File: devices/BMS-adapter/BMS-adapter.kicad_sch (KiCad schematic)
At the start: 5 parts, among them J1 Conn_01x05, J2 Conn_01x05, J3 Conn_01x02, J4 Conn_01x02, SW1 SW_SPST

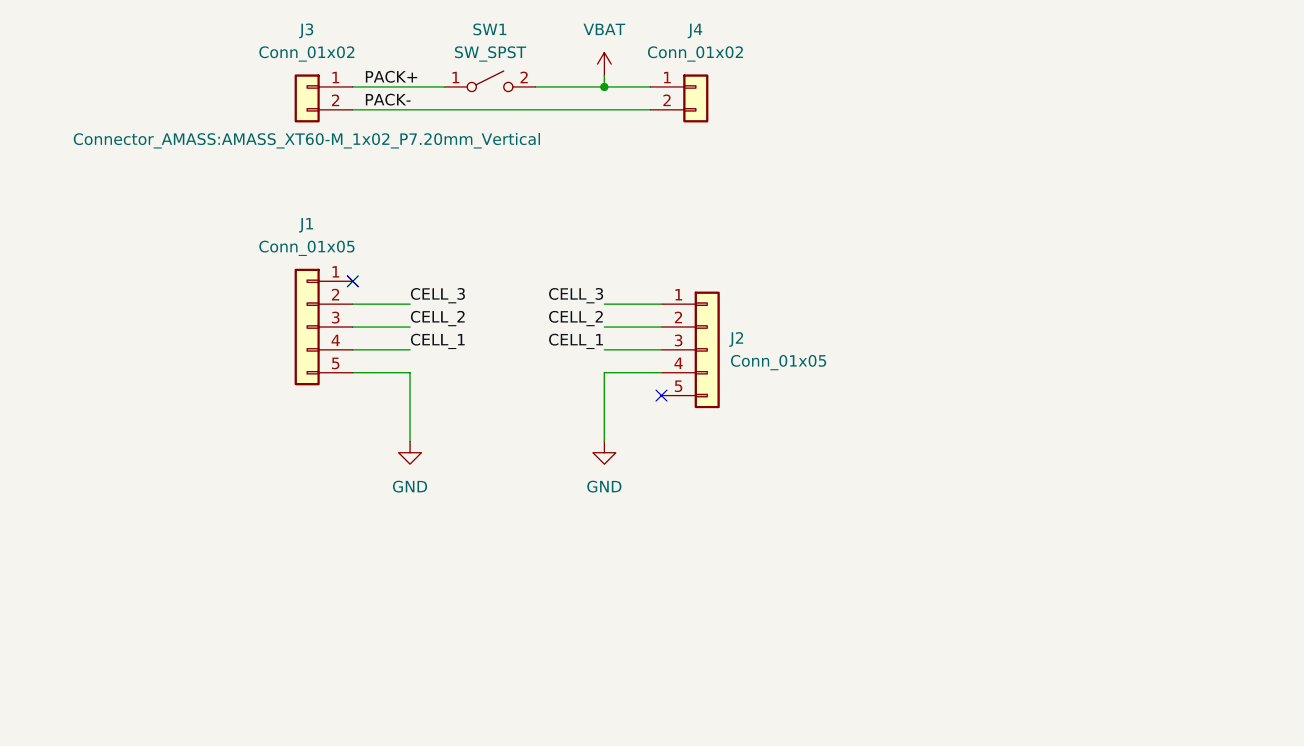
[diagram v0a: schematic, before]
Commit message: Adds a PowerJack
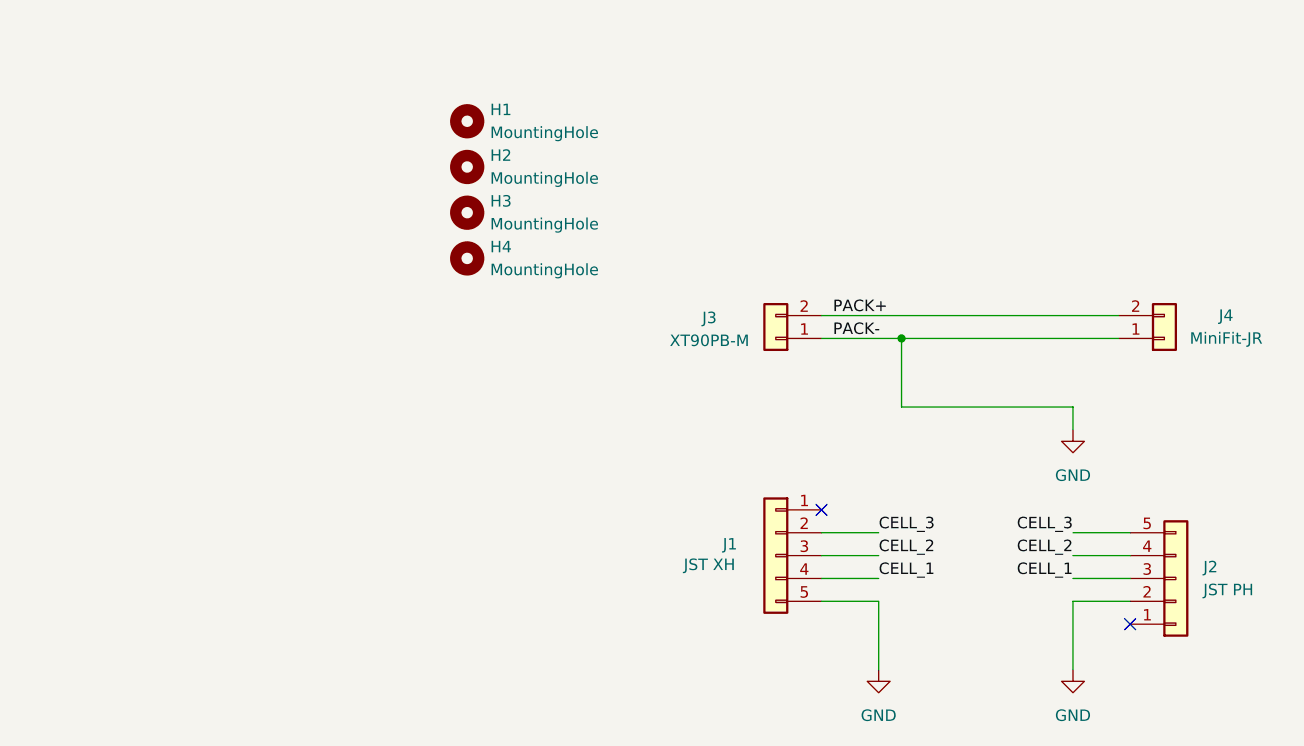
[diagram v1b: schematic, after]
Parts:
- removed SW1: SW_SPST, symbol Switch:SW_SPST
- added H1, H2, H3, H4: MountingHole, MountingHole:MountingHole_3.2mm_M3_DIN965, symbol Mechanical:MountingHole
- J1: value Conn_01x05 -> JST XH; MPN (none) -> B5B-XH-AM
- J2: value Conn_01x05 -> JST PH; MPN (none) -> B5B-PH-K
- J3: value Conn_01x02 -> XT90PB-M; footprint Connector_AMASS:AMASS_XT60-M_1x02_P7.20mm_Vertical -> common:XT90PB-M; MPN (none) -> XT90PB-M
- J4: value Conn_01x02 -> MiniFit-JR; footprint (none) -> Connector_Molex:Molex_Mini-Fit_Jr_5566-02A_2x01_P4.20mm_Vertical; MPN (none) -> 0039281023
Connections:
- net PACK- is gone; now on net PACK+: J3.2 (Pin_2), J4.2 (Pin_2)
- net VBAT is gone; now on net GND: J4.1 (Pin_1)
- net CELL_2: now also J2.4 (Pin_4); no longer J2.2 (Pin_2)
- net CELL_3: now also J2.5 (Pin_5); no longer J2.1 (Pin_1)
- net GND: now also J2.2 (Pin_2), J3.1 (Pin_1); no longer J2.4 (Pin_4)
- net PACK+: no longer J3.1 (Pin_1)
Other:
- moved on the sheet: J1, J2, J3, J4
